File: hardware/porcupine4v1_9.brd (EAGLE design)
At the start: 24.4 x 27.4 mm, 28 parts, among them X1 PROGCON

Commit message: v4.1.9: added farnell order numbers
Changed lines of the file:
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@@
 <attribute name="VALUE" x="22.8092" y="14.6304" size="1.016" layer="27" rot="R180"/>
 <attribute name="NAME" x="22.0726" y="16.2306" size="0.4064" layer="25" rot="R180"/>
-</element>
-<element name="LIGHTSENSE" library="HedgehogLib" package="TSL" value="TSL250" x="12.192" y="1.397" rot="R180"/>
+<attribute name="OC_FARNELL" value="1686452" x="24.0792" y="3.2004" size="1.778" layer="27" rot="R180" display="off"/>
+</element>
+<element name="LIGHTSENSE" library="HedgehogLib" package="TSL" value="TSL250" x="12.192" y="1.397" rot="R180">
+<attribute name="OC_FARNELL" value="1182346" x="12.192" y="1.397" size="1.778" layer="27" rot="R180" display="off"/>
+</element>
 <element name="USB_CON" library="HedgehogLib" package="248601" value="USBCON" x="18.7216" y="22.9344" smashed="yes" rot="R270">
 <attribute name="NAME" x="17.4262" y="22.0962" size="0.4064" layer="25"/>
 <attribute name="VALUE" x="11.7366" y="27.3794" size="1.27" layer="27" rot="R270"/>
+<attribute name="OC_FARNELL" value="2112367" x="18.7216" y="22.9344" size="1.778" layer="27" rot="R270" display="off"/>
 </element>
 <element name="C_PWR_VUSB" library="rcl" package="C0603K" value="1u" x="3.7024" y="17.4952" smashed="yes">
@@
 <attribute name="NAME" x="22.9616" y="9.271" size="0.4064" layer="26" rot="MR0"/>
 <attribute name="VALUE" x="22.352" y="8.9662" size="0.4064" layer="28" rot="MR0"/>
+<attribute name="OC_FARNELL" value="1853935" x="20.32" y="11.3792" size="1.778" layer="28" rot="MR0" display="off"/>
 </element>
 <element name="C_ADX_VDD" library="rcl" package="C0603K" value="0.1u" x="19.2024" y="14.0716" smashed="yes" rot="MR180">
@@
 <attribute name="NAME" x="13.2218" y="8.4108" size="0.4064" layer="26" rot="MR0"/>
 <attribute name="VALUE" x="16.3454" y="15.838" size="1.27" layer="28" rot="MR270"/>
+<attribute name="OC_FARNELL" value="1706311" x="10.8204" y="11.938" size="1.778" layer="28" rot="MR270" display="off"/>
 </element>
 <element name="C2_32KHZ" library="rcl" package="C0603K" value="22p" x="1.9304" y="4.9022" smashed="yes" rot="MR90">
@@
 </element>
 <element name="32KHZ_CRYSTAL" library="HedgehogLib" package="SMD_CRYSTAL" value="SMD_CRYSTAL" x="3.9116" y="6.985" rot="MR90">
-<attribute name="FARNELL" value="2101349" x="3.9116" y="6.985" size="1.778" layer="28" rot="MR90" display="off"/>
+<attribute name="OC_FARNELL" value="2101349" x="3.9116" y="6.985" size="1.778" layer="28" rot="MR90" display="off"/>
 </element>
 <element name="BAT" library="con-molex" package="53048-02" value="53048-02" x="2.667" y="24.3586" smashed="yes" rot="R270">
@@
 </element>
 <element name="12MHZ_RESONATOR" library="HedgehogLib" package="PRQC-C" value="RESONATORPRQC-C" x="6.477" y="3.2258" rot="MR180">
-<attribute name="DIGIKEY" value="http://www.digikey.de/product-detail/de/PRQC12.00CR5010X000/478-6318-1-ND/2506334" x="6.477" y="3.2258" size="1.778" layer="28" rot="MR180" display="off"/>
+<attribute name="OC_DIGIKEY" value="478-6318-1-ND" x="6.477" y="3.2258" size="1.778" layer="28" rot="MR180" display="off"/>
 </element>
 <element name="LDO" library="HedgehogLib" package="SOT-23-5" value="MCP1824" x="7.366" y="23.8252" smashed="yes" rot="MR90">
 <attribute name="NAME" x="7.9248" y="25.4762" size="0.4064" layer="26" rot="MR0"/>
 <attribute name="VALUE" x="4.191" y="21.9202" size="1.27" layer="28" rot="MR90"/>
+<attribute name="OC_FARNELL" value="1578387" x="7.366" y="23.8252" size="1.778" layer="28" rot="MR90" display="off"/>
 </element>
 </elements>
@@
 <wire x1="4.5352" y1="12.3304" x2="6.6576" y2="12.3304" width="0.3302" layer="1"/>
 <wire x1="9.0932" y1="0.3756" x2="7.981" y2="0.3756" width="0.3302" layer="16"/>
-<wire x1="7.981" y1="0.3756" x2="6.425746875" y2="0.376975" width="0.3302" layer="16"/>
-<wire x1="6.425746875" y1="0.376975" x2="1.8796" y2="0.381" width="0.3302" layer="16"/>
+<wire x1="7.981" y1="0.3756" x2="6.628946875" y2="0.376975" width="0.3302" layer="16"/>
 <wire x1="1.9304" y1="5.7772" x2="1.9304" y2="6.8072" width="0.3302" layer="16"/>
 <wire x1="1.9304" y1="6.8072" x2="1.952" y2="7.0498" width="0.3302" layer="16"/>
@@
 <wire x1="1.002" y1="5.7772" x2="0.7112" y2="5.4864" width="0.3302" layer="16"/>
 <wire x1="6.477" y1="3.2258" x2="6.477" y2="0.428228125" width="0.3302" layer="16"/>
-<wire x1="6.477" y1="0.428228125" x2="6.425746875" y2="0.376975" width="0.3302" layer="16"/>
-<wire x1="1.8796" y1="0.381" x2="0.7112" y2="1.5494" width="0.3302" layer="16"/>
+<wire x1="6.477" y1="0.428228125" x2="6.628946875" y2="0.376975" width="0.3302" layer="16"/>
 <wire x1="0.7112" y1="1.5494" x2="0.7112" y2="5.4864" width="0.3302" layer="16"/>
 <wire x1="5.0038" y1="25.9448" x2="11.176" y2="25.9448" width="0.3302" layer="16"/>
@@
 <wire x1="4.2926" y1="24.638" x2="4.0754" y2="24.8666" width="0.3302" layer="16"/>
 <wire x1="4.0754" y1="24.8666" x2="3.683" y2="24.624" width="0.3302" layer="16"/>
+<wire x1="6.628946875" y1="0.376975" x2="1.883625" y2="0.376975" width="0.3302" layer="16"/>
+<wire x1="1.883625" y1="0.376975" x2="0.7112" y2="1.5494" width="0.3302" layer="16"/>
 </signal>
 <signal name="USB_D+@RC5">

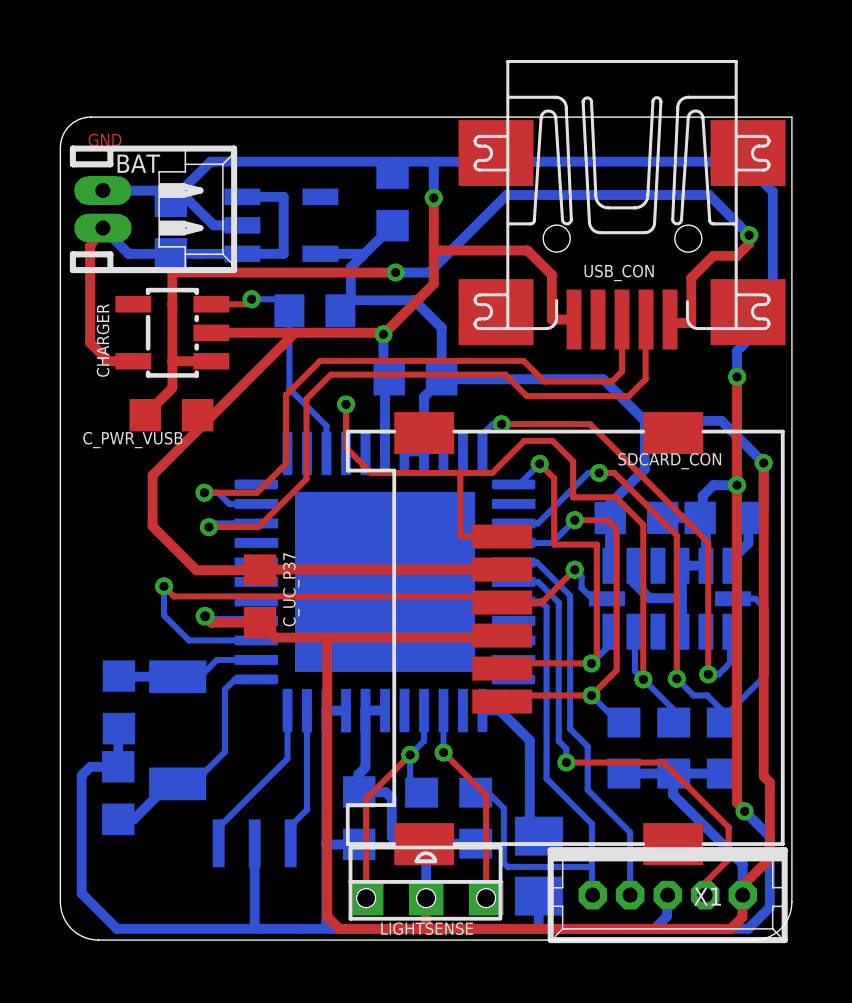
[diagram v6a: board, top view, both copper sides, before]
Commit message: updated 4v1_9 + BOM
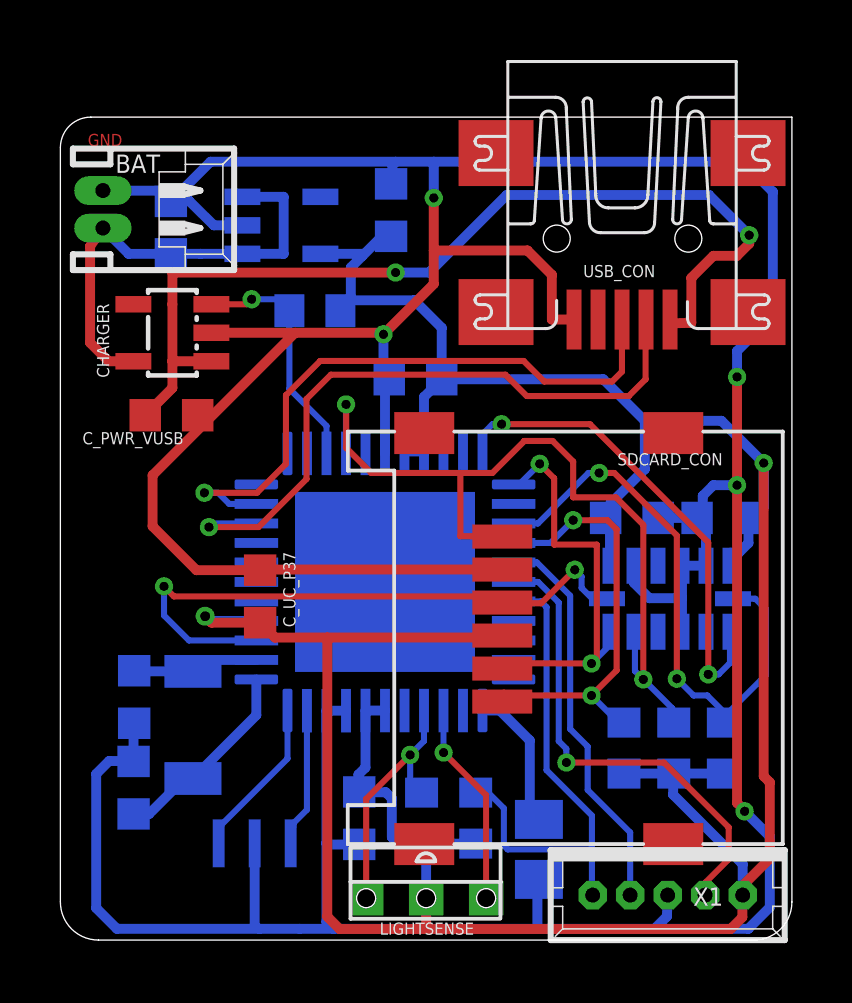
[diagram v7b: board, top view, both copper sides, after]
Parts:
- moved C_UC_VDDCORE 0.56 mm to (16.0, 3.02)
- moved C2_32KHZ 0.54 mm to (2.44, 5.08)
- moved C1_32KHZ 0.54 mm to (2.46, 8.10)
- moved 32KHZ_CRYSTAL 0.54 mm to (4.42, 7.16)
- moved C_PWR_VREG 0.36 mm to (11.0, 24.3)
- moved C_ADX_VDD 0.15 mm to (19.1, 14.1)
- moved C_ADX_VSS 0.10 mm to (22.1, 14.1)
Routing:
- net GND: track 151.6 -> 152.2 mm
- net PROG_MCLR@MCLR: track 17.4 -> 16.8 mm
- net N$6: track 4.80 -> 4.23 mm
- net N$3: track 7.70 -> 7.14 mm

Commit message: hardware basic 4.1.9 wire and BOM list update
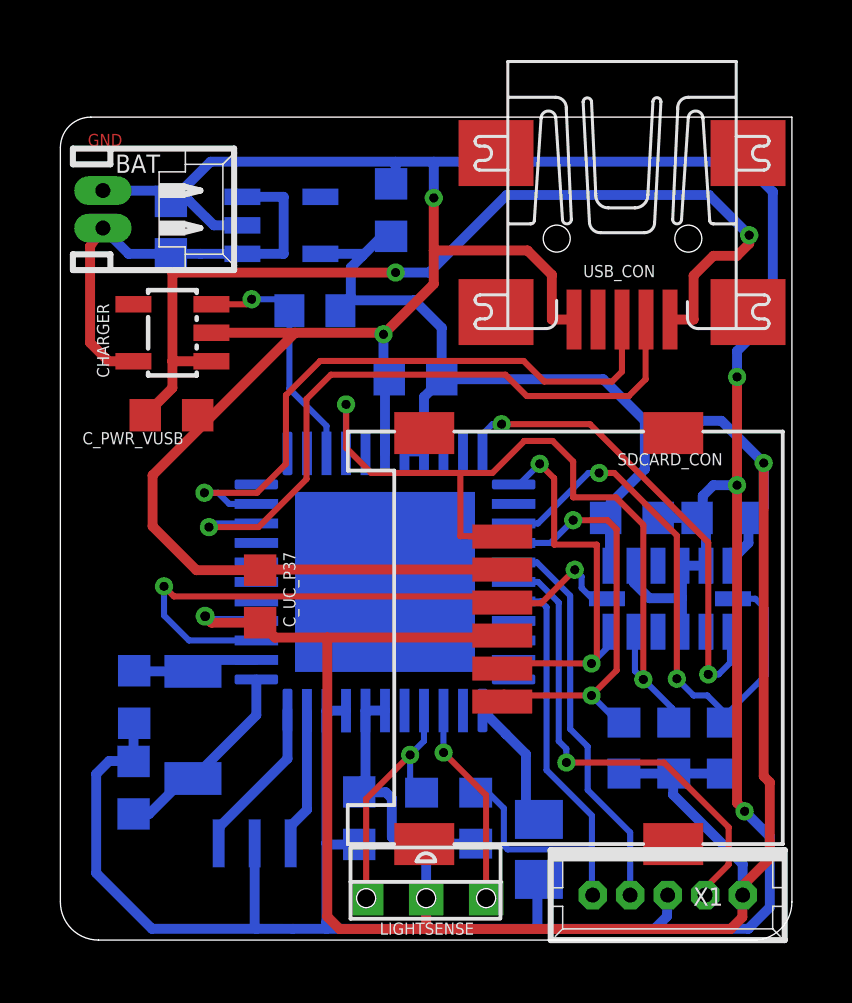
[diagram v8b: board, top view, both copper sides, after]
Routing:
- net VDDCORE: track 5.27 -> 4.41 mm
- net GND: track 152.2 -> 151.4 mm
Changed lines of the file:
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@@
 <?xml version="1.0" encoding="utf-8"?>
 <!DOCTYPE eagle SYSTEM "eagle.dtd">
-<eagle version="6.3">
+<eagle version="6.6.0">
 <drawing>
 <settings>
@@
 <wire x1="22.5552" y1="4.572" x2="22.5552" y2="15.1638" width="0.3302" layer="1"/>
 <wire x1="23.6474" y1="3.4544" x2="22.8092" y2="4.2926" width="0.3302" layer="16"/>
-<wire x1="9.0932" y1="0.3756" x2="15.9004" y2="0.3756" width="0.3302" layer="16"/>
+<wire x1="8.8646" y1="0.3756" x2="15.9004" y2="0.3756" width="0.3302" layer="16"/>
 <wire x1="15.9004" y1="0.3756" x2="19.8066" y2="0.3756" width="0.3302" layer="16"/>
 <wire x1="21.4438" y1="13.8254" x2="21.52" y2="13.8254" width="0.2032" layer="16"/>
@@
 <wire x1="23.749" y1="24.9428" x2="22.747" y2="25.9448" width="0.3302" layer="16"/>
 <wire x1="22.747" y1="25.9448" x2="12.446" y2="25.9448" width="0.3302" layer="16"/>
-<wire x1="8.8674" y1="0.607" x2="9.0932" y2="0.3756" width="0.3302" layer="16"/>
+<wire x1="8.8674" y1="0.607" x2="8.8646" y2="0.3756" width="0.3302" layer="16"/>
 <wire x1="9.9612" y1="3.189" x2="8.9096" y2="3.1836" width="0.3302" layer="16"/>
 <wire x1="8.9096" y1="3.1836" x2="8.8674" y2="3.2258" width="0.3302" layer="16"/>
@@
 <wire x1="9.5204" y1="7.6465" x2="8.8674" y2="7.6445" width="0.3302" layer="16"/>
 <wire x1="4.5352" y1="12.3304" x2="6.6576" y2="12.3304" width="0.3302" layer="1"/>
-<wire x1="9.0932" y1="0.3756" x2="7.981" y2="0.3756" width="0.3302" layer="16"/>
-<wire x1="7.981" y1="0.3756" x2="6.628946875" y2="0.376975" width="0.3302" layer="16"/>
+<wire x1="8.8646" y1="0.3756" x2="7.7524" y2="0.3756" width="0.3302" layer="16"/>
+<wire x1="7.7524" y1="0.3756" x2="6.527346875" y2="0.376975" width="0.3302" layer="16"/>
 <wire x1="2.4384" y1="5.955" x2="2.4384" y2="6.985" width="0.3302" layer="16"/>
 <wire x1="2.4384" y1="6.985" x2="2.46" y2="7.2276" width="0.3302" layer="16"/>
 <wire x1="6.477" y1="3.2258" x2="6.477" y2="0.428228125" width="0.3302" layer="16"/>
-<wire x1="6.477" y1="0.428228125" x2="6.628946875" y2="0.376975" width="0.3302" layer="16"/>
+<wire x1="6.477" y1="0.428228125" x2="6.527346875" y2="0.376975" width="0.3302" layer="16"/>
 <wire x1="5.0038" y1="25.9448" x2="11.176" y2="25.9448" width="0.3302" layer="16"/>
 <wire x1="11.176" y1="25.9448" x2="12.446" y2="25.9448" width="0.3302" layer="16"/>
-<wire x1="11.0236" y1="25.2082" x2="11.0744" y2="25.8432" width="0.3302" layer="16"/>
-<wire x1="11.0744" y1="25.8432" x2="11.176" y2="25.9448" width="0.3302" layer="16"/>
+<wire x1="11.0236" y1="25.2082" x2="11.176" y2="25.3352" width="0.3302" layer="16"/>
+<wire x1="11.176" y1="25.3352" x2="11.176" y2="25.9448" width="0.3302" layer="16"/>
 <wire x1="5.0038" y1="25.9448" x2="3.683" y2="24.624" width="0.3302" layer="16"/>
 <wire x1="3.683" y1="24.624" x2="3.3688" y2="24.9796" width="0.3302" layer="16"/>
@@
 <wire x1="4.2926" y1="24.638" x2="4.0754" y2="24.8666" width="0.3302" layer="16"/>
 <wire x1="4.0754" y1="24.8666" x2="3.683" y2="24.624" width="0.3302" layer="16"/>
-<wire x1="6.628946875" y1="0.376975" x2="1.883625" y2="0.376975" width="0.3302" layer="16"/>
+<wire x1="6.527346875" y1="0.376975" x2="3.052025" y2="0.376975" width="0.3302" layer="16"/>
 <wire x1="15.9512" y1="2.0226" x2="15.9004" y2="1.9718" width="0.3302" layer="16"/>
 <wire x1="15.9004" y1="1.9718" x2="15.9004" y2="0.3756" width="0.3302" layer="16"/>
@@
 <wire x1="2.4244" y1="5.969" x2="1.6256" y2="5.969" width="0.3302" layer="16"/>
 <wire x1="1.6256" y1="5.969" x2="1.1938" y2="5.5372" width="0.3302" layer="16"/>
-<wire x1="1.1938" y1="5.5372" x2="1.1938" y2="1.0668" width="0.3302" layer="16"/>
-<wire x1="1.1938" y1="1.0668" x2="1.883625" y2="0.376975" width="0.3302" layer="16"/>
+<wire x1="1.1938" y1="5.5372" x2="1.1938" y2="2.2352" width="0.3302" layer="16"/>
+<wire x1="1.1938" y1="2.2352" x2="3.052025" y2="0.376975" width="0.3302" layer="16"/>
 </signal>
 <signal name="USB_D+@RC5">
@@
 <contactref element="CHARGER" pad="1"/>
 <wire x1="20.3216" y1="20.6844" x2="20.32" y2="20.813" width="0.3302" layer="1"/>
-<wire x1="20.32" y1="20.559" x2="20.3216" y2="20.6844" width="0.3302" layer="1"/>
-<wire x1="21.0312" y1="20.574" x2="20.32" y2="20.559" width="0.3302" layer="1"/>
-<wire x1="21.0312" y1="22.0726" x2="21.0312" y2="20.574" width="0.3302" layer="1"/>
 <wire x1="22.9616" y1="23.495" x2="22.9616" y2="23.2156" width="0.3302" layer="1"/>
 <wire x1="22.9616" y1="23.2156" x2="22.5552" y2="22.8092" width="0.3302" layer="1"/>
 <wire x1="22.5552" y1="22.8092" x2="21.7678" y2="22.8092" width="0.3302" layer="1"/>
-<wire x1="21.7678" y1="22.8092" x2="21.0312" y2="22.0726" width="0.3302" layer="1"/>
 <via x="22.9616" y="23.495" extent="1-16" drill="0.3048" diameter="0.3048" shape="octagon"/>
 <via x="11.176" y="22.2504" extent="1-16" drill="0.3048" shape="octagon"/>
@@
 <wire x1="12.2936" y1="22.2504" x2="11.176" y2="22.2504" width="0.3302" layer="16"/>
 <wire x1="21.6154" y1="24.8412" x2="22.9616" y2="23.495" width="0.3302" layer="16"/>
-<wire x1="3.7338" y1="21.1938" x2="3.7338" y2="19.2938" width="0.3302" layer="1"/>
+<wire x1="3.7338" y1="22.2504" x2="3.7338" y2="19.2938" width="0.3302" layer="1"/>
 <wire x1="3.7338" y1="19.2938" x2="5.0338" y2="19.2938" width="0.3302" layer="1"/>
 <wire x1="11.176" y1="22.2504" x2="3.7338" y2="22.2504" width="0.3302" layer="1"/>
-<wire x1="3.7338" y1="22.2504" x2="3.7338" y2="21.1938" width="0.3302" layer="1"/>
 <wire x1="2.8274" y1="17.4952" x2="3.7338" y2="18.4016" width="0.3302" layer="1"/>
 <wire x1="3.7338" y1="18.4016" x2="3.7338" y2="19.2938" width="0.3302" layer="1"/>
+<wire x1="21.7678" y1="22.8092" x2="21.1074" y2="22.1488" width="0.3302" layer="1"/>
+<wire x1="21.1074" y1="22.1488" x2="21.1074" y2="20.6844" width="0.3302" layer="1"/>
+<wire x1="21.1074" y1="20.6844" x2="20.3216" y2="20.6844" width="0.3302" layer="1"/>
 </signal>
 <signal name="+3V3">
@@
 <wire x1="10.8204" y1="7.6505" x2="10.8194" y2="7.6515" width="0.3302" layer="16"/>
 <wire x1="10.8194" y1="7.6515" x2="10.1704" y2="7.6515" width="0.3302" layer="16"/>
-<wire x1="10.1704" y1="7.6515" x2="10.1704" y2="5.7524" width="0.3302" layer="16"/>
+<wire x1="10.1704" y1="7.6515" x2="10.1704" y2="5.3968" width="0.3302" layer="16"/>
 <wire x1="9.3336" y1="20.9804" x2="9.6821" y2="21.3271" width="0.3302" layer="16"/>
 <wire x1="8.8968" y1="10.0838" x2="14.6626" y2="10.0838" width="0.3302" layer="1"/>
@@
 <wire x1="12.7114" y1="18.6944" x2="12.1204" y2="18.1034" width="0.3302" layer="16"/>
 <wire x1="12.1204" y1="18.1034" x2="12.1204" y2="16.2255" width="0.3302" layer="16"/>
-<wire x1="9.9612" y1="4.939" x2="9.9358" y2="5.5178" width="0.3302" layer="16"/>
-<wire x1="9.9358" y1="5.5178" x2="10.1704" y2="5.7524" width="0.3302" layer="16"/>
+<wire x1="9.9612" y1="4.939" x2="9.9612" y2="5.1876" width="0.3302" layer="16"/>
+<wire x1="9.9612" y1="5.1876" x2="10.1704" y2="5.3968" width="0.3302" layer="16"/>
 <wire x1="10.0314" y1="5.0292" x2="9.9612" y2="4.939" width="0.3302" layer="16"/>
 <wire x1="12.0396" y1="3.214" x2="11.264" y2="3.214" width="0.3302" layer="16"/>
@@
 <wire x1="22.2758" y1="3.7592" x2="20.1168" y2="5.9182" width="0.2032" layer="1"/>
 <via x="16.8656" y="5.9182" extent="1-16" drill="0.3048" shape="octagon"/>
-<wire x1="22.2758" y1="3.7592" x2="22.2758" y2="2.6924" width="0.2032" layer="1"/>
-<wire x1="22.2758" y1="2.6924" x2="21.4938" y2="1.9104" width="0.2032" layer="1"/>
-<wire x1="21.4938" y1="1.9104" x2="21.4938" y2="1.4986" width="0.2032" layer="1"/>
+<wire x1="22.2758" y1="3.7592" x2="22.2758" y2="2.5146" width="0.2032" layer="1"/>
+<wire x1="22.2758" y1="2.5146" x2="21.4938" y2="1.7326" width="0.2032" layer="1"/>
+<wire x1="21.4938" y1="1.7326" x2="21.4938" y2="1.4986" width="0.2032" layer="1"/>
 </signal>
 <signal name="SDI">
@@
 <contactref element="PIC_CONTROLLER" pad="23"/>
 <contactref element="C_UC_VDDCORE" pad="1"/>
-<wire x1="15.9512" y1="4.0226" x2="15.6464" y2="3.7686" width="0.3302" layer="16"/>
-<wire x1="15.6464" y1="3.7686" x2="15.6464" y2="6.6548" width="0.3302" layer="16"/>
-<wire x1="15.6464" y1="6.6548" x2="14.6477" y2="7.6535" width="0.3302" layer="16"/>
-<wire x1="14.6477" y1="7.6535" x2="14.0704" y2="7.6535" width="0.3302" layer="16"/>
+<wire x1="15.9512" y1="4.0226" x2="15.5194" y2="4.4544" width="0.3302" layer="16"/>
+<wire x1="15.5194" y1="4.4544" x2="15.5194" y2="6.1976" width="0.3302" layer="16"/>
+<wire x1="15.5194" y1="6.1976" x2="14.8509" y2="6.8661" width="0.3302" layer="16"/>
+<wire x1="14.8509" y1="6.8661" x2="14.0704" y2="7.6535" width="0.3302" layer="16"/>
 </signal>
 <signal name="PROG_MCLR@MCLR">
@@
 <signal name="N$1">
 <contactref element="PIC_CONTROLLER" pad="32"/>
-<wire x1="8.2184" y1="4.3434" x2="8.2184" y2="7.6455" width="0.2032" layer="16"/>
+<wire x1="8.2184" y1="4.3434" x2="8.2184" y2="7.6455" width="0.3302" layer="16"/>
 <contactref element="12MHZ_RESONATOR" pad="3"/>
-<wire x1="7.677" y1="3.2258" x2="7.7786" y2="3.9036" width="0.2032" layer="16"/>
-<wire x1="7.7786" y1="3.9036" x2="8.2184" y2="4.3434" width="0.2032" layer="16"/>
+<wire x1="7.677" y1="3.2258" x2="7.677" y2="3.802" width="0.3302" layer="16"/>
+<wire x1="7.677" y1="3.802" x2="8.2184" y2="4.3434" width="0.3302" layer="16"/>
 </signal>
 <signal name="N$2">
 <contactref element="PIC_CONTROLLER" pad="33"/>
 <contactref element="12MHZ_RESONATOR" pad="1"/>
-<wire x1="7.5704" y1="7.6535" x2="7.5704" y2="6.0464" width="0.2032" layer="16"/>
-<wire x1="7.5704" y1="6.0464" x2="5.2894" y2="3.7654" width="0.2032" layer="16"/>
-<wire x1="5.2894" y1="3.7654" x2="5.277" y2="3.2258" width="0.2032" layer="16"/>
+<wire x1="7.5704" y1="7.6535" x2="7.5704" y2="6.0464" width="0.3302" layer="16"/>
+<wire x1="7.5704" y1="6.0464" x2="5.2894" y2="3.7654" width="0.3302" layer="16"/>
+<wire x1="5.2894" y1="3.7654" x2="5.277" y2="3.2258" width="0.3302" layer="16"/>
 </signal>
 <signal name="L_GND@RE0">
